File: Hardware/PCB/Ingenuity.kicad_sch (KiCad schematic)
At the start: 38 parts, among them J1 Conn_ST_STDC14, J2 Conn_02x20_Odd_Even, J3 Conn_02x05_Odd_Even, J4 Conn_01x02, J5 Conn_01x02, J7 Conn_01x03, J8 Conn_01x03, J9 Conn_01x02, Q1 NMOS, Q2 NMOS, SW1 SW_SPDT, U1 STM32L412KBTx, U3 LSM6DSM, U4 AMS1117-3.3

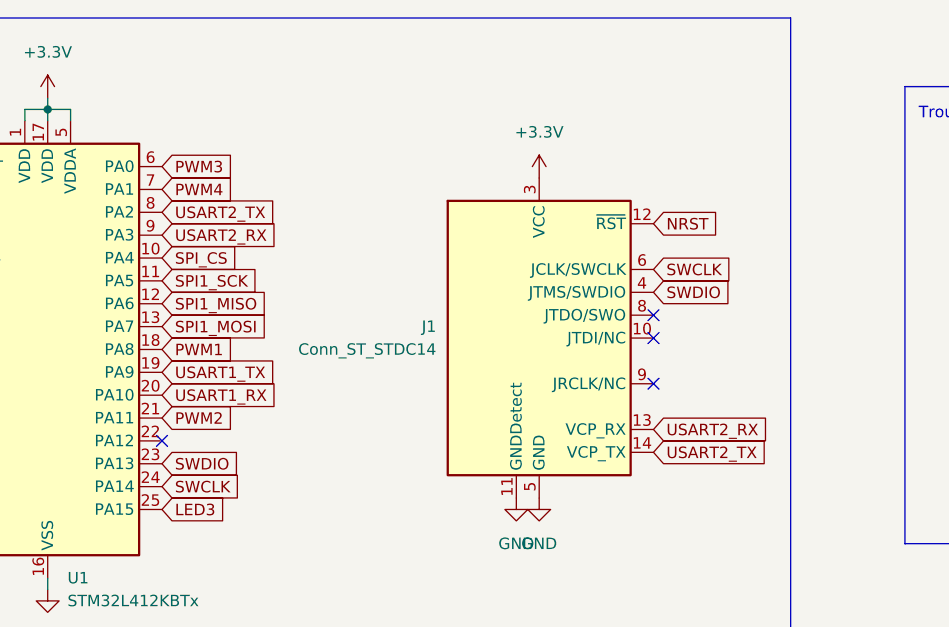
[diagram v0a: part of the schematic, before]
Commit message: update schematic, switch pins, change zones and routing
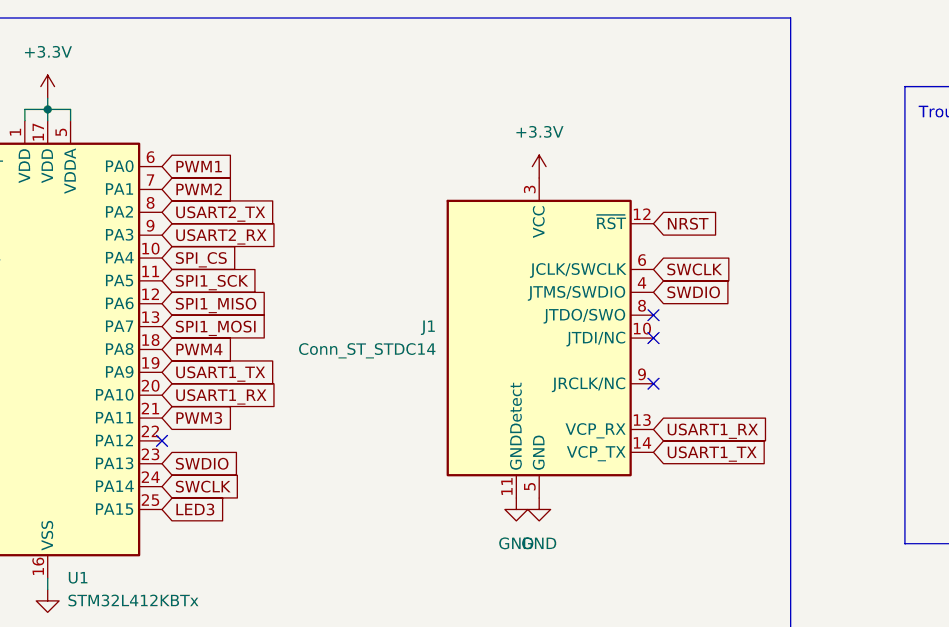
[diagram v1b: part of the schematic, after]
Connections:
- net PWM1: now also U1.6 (PA0); no longer U1.18 (PA8)
- net PWM2: now also U1.7 (PA1); no longer U1.21 (PA11)
- net PWM3: now also U1.21 (PA11); no longer U1.6 (PA0)
- net PWM4: now also U1.18 (PA8); no longer U1.7 (PA1)
- net USART1_RX: now also J1.13 (VCP_RX)
- net USART1_TX: now also J1.14 (VCP_TX)
- net USART2_RX: no longer J1.13 (VCP_RX)
- net USART2_TX: no longer J1.14 (VCP_TX)

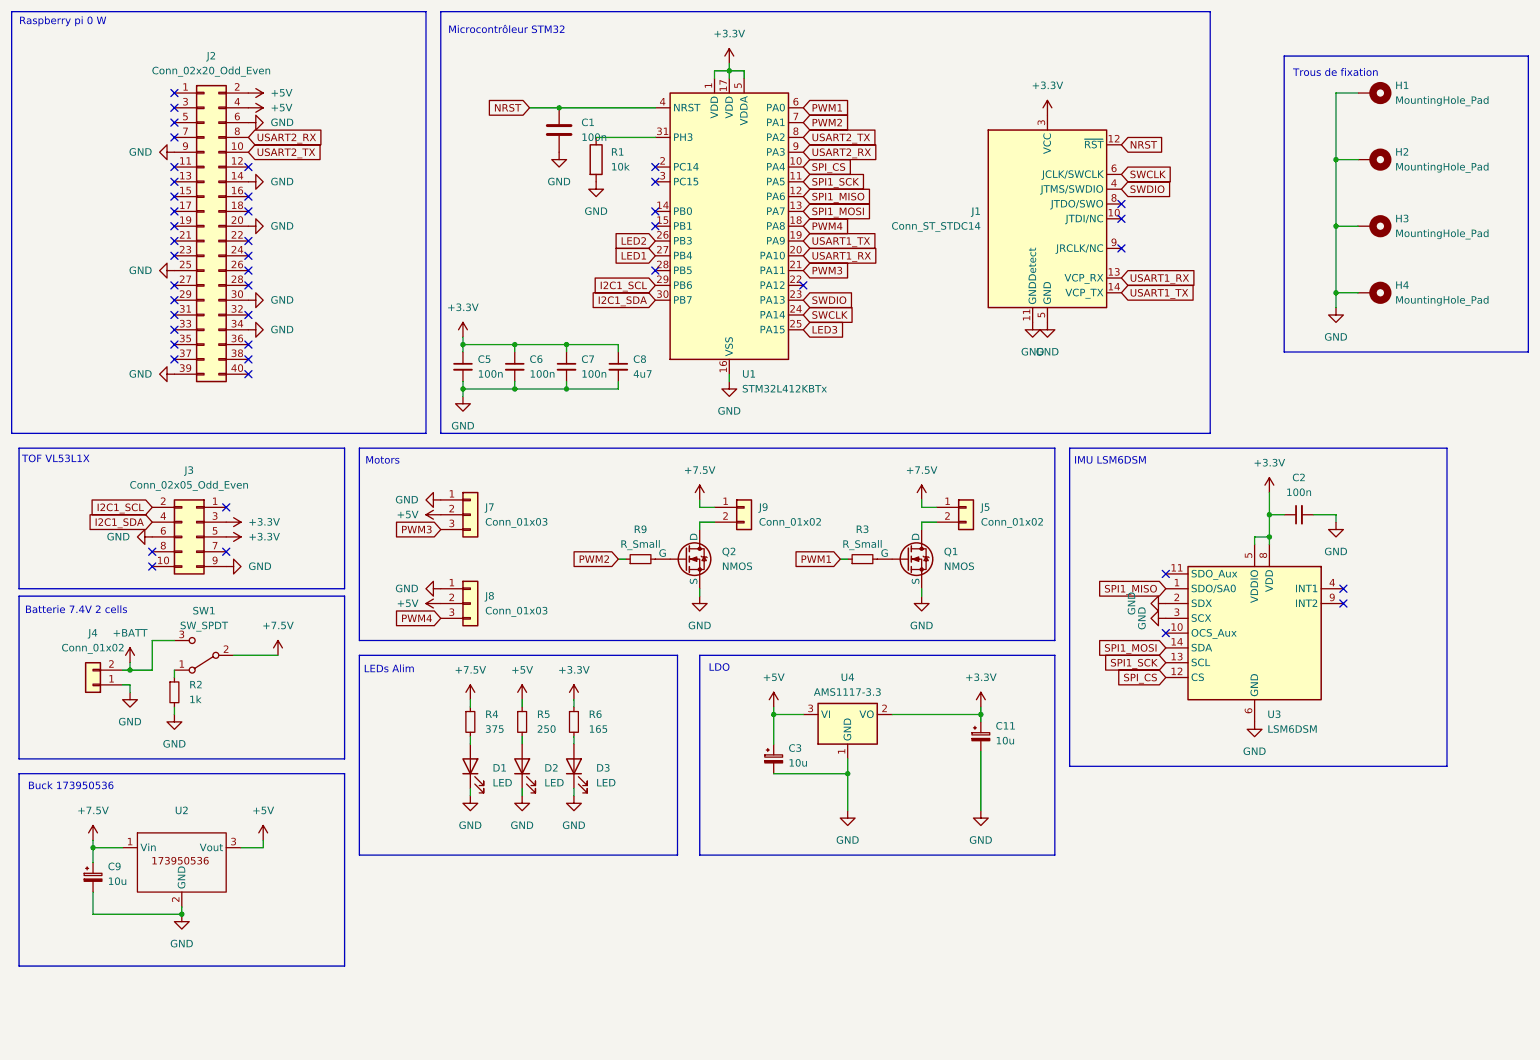
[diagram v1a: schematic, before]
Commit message: add led, button
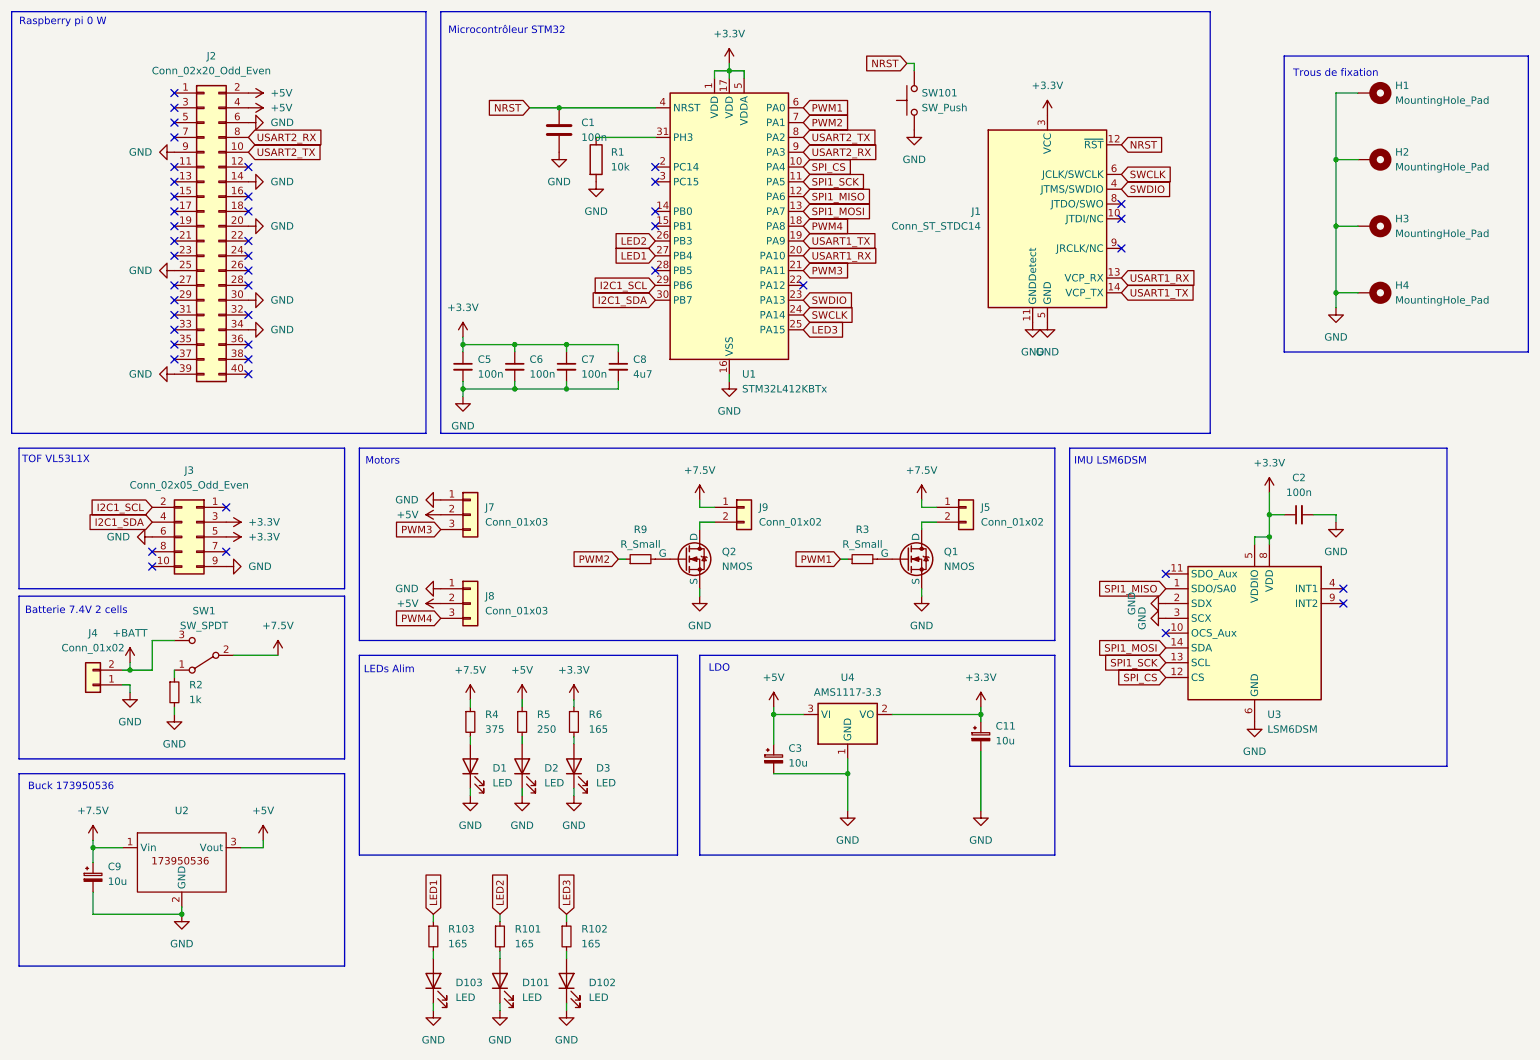
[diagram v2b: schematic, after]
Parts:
- added D101, D102, D103: LED, LED_SMD:LED_0603_1608Metric, symbol Device:LED
- added R101, R102, R103: 165, Resistor_SMD:R_0402_1005Metric, symbol Device:R_Small
- added SW101: SW_Push, Button_Switch_SMD:SW_Push_1P1T_NO_6x6mm_H9.5mm, symbol Switch:SW_Push
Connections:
- net GND: now also D101.1 (K), D102.1 (K), D103.1 (K), SW101.1
- net LED1: now also R103.1
- net LED2: now also R101.1
- net LED3: now also R102.1
- net NRST: now also SW101.2
- new net: D101.2 (A), R101.2
- new net: D103.2 (A), R103.2
- new net: D102.2 (A), R102.2

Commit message: finalize pcb
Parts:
- renumbered C9 to C1, C5 to C2, C6 to C3, C1 to C4, C7 to C5, C8 to C6, C3 to C7, C11 to C8, C2 to C9, D103 to D1, D1 to D2, D101 to D3, D2 to D4, D102 to D5, D3 to D6, J4 to J1, J3 to J2, J2 to J3, J7 to J4, J8 to J5, J9 to J6, J5 to J7, J1 to J8, Q2 to Q1, Q1 to Q2, R2 to R1, R3 to R10, R103 to R2, R4 to R3, R101 to R4, R102 to R6, R6 to R7, R1 to R8, SW101 to SW2, U2 to U1, U1 to U2, U4 to U3, U3 to U4
